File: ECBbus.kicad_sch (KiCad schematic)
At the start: 1 part, among them P1 C96ABC

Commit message: Schematic in progress
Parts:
- removed P1: C96ABC, C96ABCMC, symbol 6x0x-6U-rescue:C96ABC
- added J1, J15, J17, J19, J21: IRQ Selection, Connector_PinHeader_2.54mm:PinHeader_2x06_P2.54mm_Vertical, symbol Connector_Generic:Conn_02x06_Counter_Clockwise
- added J16, J18, J2, J20, J22: Bus_ISA_8bit, Custom:BUSPC_HOST, symbol Custom:Bus_ISA_8bit_CUSTOM
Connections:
- net B_/CLK: now also J16.20 (CLK), J18.20 (CLK), J2.20 (CLK), J20.20 (CLK), J22.20 (CLK)
- net B_/NMI: now also J16.32 (IO), J18.32 (IO), J2.32 (IO), J20.32 (IO), J22.32 (IO)
- net B_A0: now also J16.62 (BA00), J18.62 (BA00), J2.62 (BA00), J20.62 (BA00), J22.62 (BA00)
- net B_A1: now also J16.61 (BA01), J18.61 (BA01), J2.61 (BA01), J20.61 (BA01), J22.61 (BA01)
- net B_A10: now also J16.52 (BA10), J18.52 (BA10), J2.52 (BA10), J20.52 (BA10), J22.52 (BA10)
- net B_A11: now also J16.51 (BA11), J18.51 (BA11), J2.51 (BA11), J20.51 (BA11), J22.51 (BA11)
- net B_A12: now also J16.50 (BA12), J18.50 (BA12), J2.50 (BA12), J20.50 (BA12), J22.50 (BA12)
- net B_A13: now also J16.49 (BA13), J18.49 (BA13), J2.49 (BA13), J20.49 (BA13), J22.49 (BA13)
- net B_A14: now also J16.48 (BA14), J18.48 (BA14), J2.48 (BA14), J20.48 (BA14), J22.48 (BA14)
- net B_A15: now also J16.47 (BA15), J18.47 (BA15), J2.47 (BA15), J20.47 (BA15), J22.47 (BA15)
- net B_A16: now also J16.46 (BA16), J18.46 (BA16), J2.46 (BA16), J20.46 (BA16), J22.46 (BA16)
- net B_A17: now also J16.45 (BA17), J18.45 (BA17), J2.45 (BA17), J20.45 (BA17), J22.45 (BA17)
- net B_A18: now also J16.44 (BA18), J18.44 (BA18), J2.44 (BA18), J20.44 (BA18), J22.44 (BA18)
- net B_A19: now also J16.43 (BA19), J18.43 (BA19), J2.43 (BA19), J20.43 (BA19), J22.43 (BA19)
- net B_A2: now also J16.60 (BA02), J18.60 (BA02), J2.60 (BA02), J20.60 (BA02), J22.60 (BA02)
- net B_A3: now also J16.59 (BA03), J18.59 (BA03), J2.59 (BA03), J20.59 (BA03), J22.59 (BA03)
- net B_A4: now also J16.58 (BA04), J18.58 (BA04), J2.58 (BA04), J20.58 (BA04), J22.58 (BA04)
- net B_A5: now also J16.57 (BA05), J18.57 (BA05), J2.57 (BA05), J20.57 (BA05), J22.57 (BA05)
- net B_A6: now also J16.56 (BA06), J18.56 (BA06), J2.56 (BA06), J20.56 (BA06), J22.56 (BA06)
- net B_A7: now also J16.55 (BA07), J18.55 (BA07), J2.55 (BA07), J20.55 (BA07), J22.55 (BA07)
- net B_A8: now also J16.54 (BA08), J18.54 (BA08), J2.54 (BA08), J20.54 (BA08), J22.54 (BA08)
- net B_A9: now also J16.53 (BA09), J18.53 (BA09), J2.53 (BA09), J20.53 (BA09), J22.53 (BA09)
- net B_D0: now also J16.40 (DB0), J18.40 (DB0), J2.40 (DB0), J20.40 (DB0), J22.40 (DB0)
- net B_D1: now also J16.39 (DB1), J18.39 (DB1), J2.39 (DB1), J20.39 (DB1), J22.39 (DB1)
- net B_D2: now also J16.38 (DB2), J18.38 (DB2), J2.38 (DB2), J20.38 (DB2), J22.38 (DB2)
- net B_D3: now also J16.37 (DB3), J18.37 (DB3), J2.37 (DB3), J20.37 (DB3), J22.37 (DB3)
- net B_D4: now also J16.36 (DB4), J18.36 (DB4), J2.36 (DB4), J20.36 (DB4), J22.36 (DB4)
- net B_D5: now also J16.35 (DB5), J18.35 (DB5), J2.35 (DB5), J20.35 (DB5), J22.35 (DB5)
- net B_D6: now also J16.34 (DB6), J18.34 (DB6), J2.34 (DB6), J20.34 (DB6), J22.34 (DB6)
- net B_D7: now also J16.33 (DB7), J18.33 (DB7), J2.33 (DB7), J20.33 (DB7), J22.33 (DB7)
- net GND: now also J16.1 (GND), J16.10 (GND), J16.31 (GND), J18.1 (GND), J18.10 (GND), J18.31 (GND), J2.1 (GND), J2.10 (GND), J2.31 (GND), J20.1 (GND), J20.10 (GND), J20.31 (GND), J22.1 (GND), J22.10 (GND), J22.31 (GND)
- net VCC: now also J16.29 (VCC), J16.3 (VCC), J18.29 (VCC), J18.3 (VCC), J2.29 (VCC), J2.3 (VCC), J20.29 (VCC), J20.3 (VCC), J22.29 (VCC), J22.3 (VCC)
- new net: J21.10 (Pin_10), J22.23 (IRQ5)
- new net: J21.11 (Pin_11), J22.22 (IRQ6)
- new net: J21.12 (Pin_12), J22.21 (IRQ7)
- new net: J21.8 (Pin_8), J22.25 (IRQ3)
- new net: J21.9 (Pin_9), J22.24 (IRQ4)
- new net: J15.12 (Pin_12), J16.21 (IRQ7)
- new net: J15.11 (Pin_11), J16.22 (IRQ6)
- new net: J15.10 (Pin_10), J16.23 (IRQ5)
- new net: J15.9 (Pin_9), J16.24 (IRQ4)
- new net: J15.8 (Pin_8), J16.25 (IRQ3)
- new net: J1.12 (Pin_12), J2.21 (IRQ7)
- new net: J1.11 (Pin_11), J2.22 (IRQ6)
- new net: J1.10 (Pin_10), J2.23 (IRQ5)
- new net: J1.9 (Pin_9), J2.24 (IRQ4)
- new net: J1.8 (Pin_8), J2.25 (IRQ3)
- new net: J19.10 (Pin_10), J20.23 (IRQ5)
- new net: J19.11 (Pin_11), J20.22 (IRQ6)
- new net: J19.12 (Pin_12), J20.21 (IRQ7)
- new net: J19.8 (Pin_8), J20.25 (IRQ3)
- new net: J19.9 (Pin_9), J20.24 (IRQ4)
- new net: J17.10 (Pin_10), J18.23 (IRQ5)
- new net: J17.11 (Pin_11), J18.22 (IRQ6)
- new net: J17.12 (Pin_12), J18.21 (IRQ7)
- new net: J17.8 (Pin_8), J18.25 (IRQ3)
- new net: J17.9 (Pin_9), J18.24 (IRQ4)
- new net +12V: J16.9 (+12V), J18.9 (+12V), J2.9 (+12V), J20.9 (+12V), J22.9 (+12V)
- new net -12V: J16.7 (-12V), J18.7 (-12V), J2.7 (-12V), J20.7 (-12V), J22.7 (-12V)
- new net -5V: J16.5 (-5V), J18.5 (-5V), J2.5 (-5V), J20.5 (-5V), J22.5 (-5V)
- new net BUSALE: J16.28 (ALE), J18.28 (ALE), J2.28 (ALE), J20.28 (ALE), J22.28 (ALE)
- new net BUSCLK: J16.30 (OSC), J18.30 (OSC), J2.30 (OSC), J20.30 (OSC), J22.30 (OSC)
- new net B_INT: J1.1 (Pin_1), J1.2 (Pin_2), J1.3 (Pin_3), J1.4 (Pin_4), J1.5 (Pin_5), J1.6 (Pin_6), J15.1 (Pin_1), J15.2 (Pin_2), J15.3 (Pin_3), J15.4 (Pin_4), J15.5 (Pin_5), J15.6 (Pin_6), J17.1 (Pin_1), J17.2 (Pin_2), J17.3 (Pin_3), J17.4 (Pin_4), J17.5 (Pin_5), J17.6 (Pin_6), J19.1 (Pin_1), J19.2 (Pin_2), J19.3 (Pin_3), J19.4 (Pin_4), J19.5 (Pin_5), J19.6 (Pin_6), J21.1 (Pin_1), J21.2 (Pin_2), J21.3 (Pin_3), J21.4 (Pin_4), J21.5 (Pin_5), J21.6 (Pin_6)
- new net IOR: J16.14 (~{IOR}), J18.14 (~{IOR}), J2.14 (~{IOR}), J20.14 (~{IOR}), J22.14 (~{IOR})
- new net IOW: J16.13 (~{IOW}), J18.13 (~{IOW}), J2.13 (~{IOW}), J20.13 (~{IOW}), J22.13 (~{IOW})
- new net SMEMR: J16.12 (~{SMEMR}), J18.12 (~{SMEMR}), J2.12 (~{SMEMR}), J20.12 (~{SMEMR}), J22.12 (~{SMEMR})
- new net SMEMW: J16.11 (~{SMEMW}), J18.11 (~{SMEMW}), J2.11 (~{SMEMW}), J20.11 (~{SMEMW}), J22.11 (~{SMEMW})
- new net isa_iq_1: J17.7 (Pin_7), J18.4 (IRQ2)
- new net isa_iq_2: J15.7 (Pin_7), J16.4 (IRQ2)
- new net isa_iq_3: J1.7 (Pin_7), J2.4 (IRQ2)
- new net isa_iq_4: J19.7 (Pin_7), J20.4 (IRQ2)
- new net isa_iq_5: J21.7 (Pin_7), J22.4 (IRQ2)
- new net /RESET: J16.2 (RESET), J18.2 (RESET), J2.2 (RESET), J20.2 (RESET), J22.2 (RESET)
- no-connect marks 41 -> 55
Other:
- company: N8VEM Users Group -> (none)
- title: 6809 and 6502 ATX and 6U -> 6809PC

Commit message: PCB in progress
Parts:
- J1: renamed from J21; footprint Connector_PinHeader_2.54mm:PinHeader_2x06_P2.54mm_Vertical -> Custom:STD_DDW_PINHEAD_V_2x06
- J2: renamed from J17; footprint Connector_PinHeader_2.54mm:PinHeader_2x06_P2.54mm_Vertical -> Custom:STD_DDW_PINHEAD_V_2x06
- J5: renamed from J15; footprint Connector_PinHeader_2.54mm:PinHeader_2x06_P2.54mm_Vertical -> Custom:STD_DDW_PINHEAD_V_2x06
- J7: renamed from J1; footprint Connector_PinHeader_2.54mm:PinHeader_2x06_P2.54mm_Vertical -> Custom:STD_DDW_PINHEAD_V_2x06
- J9: renamed from J19; footprint Connector_PinHeader_2.54mm:PinHeader_2x06_P2.54mm_Vertical -> Custom:STD_DDW_PINHEAD_V_2x06
- renumbered J20 to J10, J22 to J3, J18 to J4, J16 to J6, J2 to J8

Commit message: PCB
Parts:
- J1, J2, J5, J7, J9: symbol Connector_Generic:Conn_02x06_Counter_Clockwise -> Connector_Generic:Conn_02x06_Odd_Even
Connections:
- net B_INT: now also J1.11 (Pin_11), J1.7 (Pin_7), J1.9 (Pin_9), J2.11 (Pin_11), J2.7 (Pin_7), J2.9 (Pin_9), J5.11 (Pin_11), J5.7 (Pin_7), J5.9 (Pin_9), J7.11 (Pin_11), J7.7 (Pin_7), J7.9 (Pin_9), J9.11 (Pin_11), J9.7 (Pin_7), J9.9 (Pin_9); no longer J1.2 (Pin_2), J1.4 (Pin_4), J1.6 (Pin_6), J2.2 (Pin_2), J2.4 (Pin_4), J2.6 (Pin_6), J5.2 (Pin_2), J5.4 (Pin_4), J5.6 (Pin_6), J7.2 (Pin_2), J7.4 (Pin_4), J7.6 (Pin_6), J9.2 (Pin_2), J9.4 (Pin_4), J9.6 (Pin_6)
- net isa_iq_1: now also J2.12 (Pin_12); no longer J2.7 (Pin_7)
- net isa_iq_2: now also J5.12 (Pin_12); no longer J5.7 (Pin_7)
- net isa_iq_3: now also J7.12 (Pin_12); no longer J7.7 (Pin_7)
- net isa_iq_4: now also J9.12 (Pin_12); no longer J9.7 (Pin_7)
- net isa_iq_5: now also J1.12 (Pin_12); no longer J1.7 (Pin_7)
- net at J1.10 (Pin_10): now also J3.25 (IRQ3); no longer J3.23 (IRQ5)
- net at J3.22 (IRQ6): now also J1.4 (Pin_4); no longer J1.11 (Pin_11)
- net at J3.21 (IRQ7): now also J1.2 (Pin_2); no longer J1.12 (Pin_12)
- net at J1.8 (Pin_8): now also J3.24 (IRQ4); no longer J3.25 (IRQ3)
- net at J6.21 (IRQ7): now also J5.2 (Pin_2); no longer J5.12 (Pin_12)
- net at J6.22 (IRQ6): now also J5.4 (Pin_4); no longer J5.11 (Pin_11)
- net at J6.23 (IRQ5): now also J5.6 (Pin_6); no longer J5.10 (Pin_10)
- net at J6.24 (IRQ4): now also J5.8 (Pin_8); no longer J5.9 (Pin_9)
- net at J6.25 (IRQ3): now also J5.10 (Pin_10); no longer J5.8 (Pin_8)
- net at J8.21 (IRQ7): now also J7.2 (Pin_2); no longer J7.12 (Pin_12)
- net at J8.22 (IRQ6): now also J7.4 (Pin_4); no longer J7.11 (Pin_11)
- net at J8.23 (IRQ5): now also J7.6 (Pin_6); no longer J7.10 (Pin_10)
- net at J8.24 (IRQ4): now also J7.8 (Pin_8); no longer J7.9 (Pin_9)
- net at J8.25 (IRQ3): now also J7.10 (Pin_10); no longer J7.8 (Pin_8)
- net at J9.10 (Pin_10): now also J10.25 (IRQ3); no longer J10.23 (IRQ5)
- net at J10.22 (IRQ6): now also J9.4 (Pin_4); no longer J9.11 (Pin_11)
- net at J10.21 (IRQ7): now also J9.2 (Pin_2); no longer J9.12 (Pin_12)
- net at J9.8 (Pin_8): now also J10.24 (IRQ4); no longer J10.25 (IRQ3)
- net at J2.10 (Pin_10): now also J4.25 (IRQ3); no longer J4.23 (IRQ5)
- net at J4.22 (IRQ6): now also J2.4 (Pin_4); no longer J2.11 (Pin_11)
- net at J4.21 (IRQ7): now also J2.2 (Pin_2); no longer J2.12 (Pin_12)
- net at J2.8 (Pin_8): now also J4.24 (IRQ4); no longer J4.25 (IRQ3)
- new net: J1.6 (Pin_6), J3.23 (IRQ5)
- new net: J10.23 (IRQ5), J9.6 (Pin_6)
- new net: J2.6 (Pin_6), J4.23 (IRQ5)
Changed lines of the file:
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@@
 	)
 	(symbol
-		(lib_id "Connector_Generic:Conn_02x06_Counter_Clockwise")
+		(lib_id "Connector_Generic:Conn_02x06_Odd_Even")
 		(at 35.56 177.8 0)
 		(unit 1)
@@
 			)
 		)
-		(property "Description" "Generic connector, double row, 02x06, counter clockwise pin numbering scheme (similar to DIP package numbering), script generated (kicad-library-utils/schlib/autogen/connector/)"
+		(property "Description" "Generic connector, double row, 02x06, odd/even pin numbering scheme (row 1 odd numbers, row 2 even numbers), script generated (kicad-library-utils/schlib/autogen/connector/)"
 			(at 35.56 177.8 0)
 			(effects
@@
 	)
 	(symbol
-		(lib_id "Connector_Generic:Conn_02x06_Counter_Clockwise")
+		(lib_id "Connector_Generic:Conn_02x06_Odd_Even")
 		(at 322.58 78.74 0)
 		(unit 1)
@@
 			)
 		)
-		(property "Description" "Generic connector, double row, 02x06, counter clockwise pin numbering scheme (similar to DIP package numbering), script generated (kicad-library-utils/schlib/autogen/connector/)"
+		(property "Description" "Generic connector, double row, 02x06, odd/even pin numbering scheme (row 1 odd numbers, row 2 even numbers), script generated (kicad-library-utils/schlib/autogen/connector/)"
 			(at 322.58 78.74 0)
 			(effects
@@
 	)
 	(symbol
-		(lib_id "Connector_Generic:Conn_02x06_Counter_Clockwise")
+		(lib_id "Connector_Generic:Conn_02x06_Odd_Even")
 		(at 226.06 78.74 0)
 		(unit 1)
@@
 			)
 		)
-		(property "Description" "Generic connector, double row, 02x06, counter clockwise pin numbering scheme (similar to DIP package numbering), script generated (kicad-library-utils/schlib/autogen/connector/)"
+		(property "Description" "Generic connector, double row, 02x06, odd/even pin numbering scheme (row 1 odd numbers, row 2 even numbers), script generated (kicad-library-utils/schlib/autogen/connector/)"
 			(at 226.06 78.74 0)
 			(effects
@@
 	)
 	(symbol
-		(lib_id "Connector_Generic:Conn_02x06_Counter_Clockwise")
+		(lib_id "Connector_Generic:Conn_02x06_Odd_Even")
 		(at 36.83 81.28 0)
 		(unit 1)
@@
 			)
 		)
-		(property "Description" "Generic connector, double row, 02x06, counter clockwise pin numbering scheme (similar to DIP package numbering), script generated (kicad-library-utils/schlib/autogen/connector/)"
+		(property "Description" "Generic connector, double row, 02x06, odd/even pin numbering scheme (row 1 odd numbers, row 2 even numbers), script generated (kicad-library-utils/schlib/autogen/connector/)"
 			(at 36.83 81.28 0)
 			(effects
@@
 	)
 	(symbol
-		(lib_id "Connector_Generic:Conn_02x06_Counter_Clockwise")
+		(lib_id "Connector_Generic:Conn_02x06_Odd_Even")
 		(at 130.81 80.01 0)
 		(unit 1)
@@
 			)
 		)
-		(property "Description" "Generic connector, double row, 02x06, counter clockwise pin numbering scheme (similar to DIP package numbering), script generated (kicad-library-utils/schlib/autogen/connector/)"
+		(property "Description" "Generic connector, double row, 02x06, odd/even pin numbering scheme (row 1 odd numbers, row 2 even numbers), script generated (kicad-library-utils/schlib/autogen/connector/)"
 			(at 130.81 80.01 0)
 			(effects

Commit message: V1.1
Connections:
- net TC: now reaches J3.27 (TC)
- net TC: now also J10.27 (TC), J4.27 (TC), J6.27 (TC), J8.27 (TC)
- no-connect marks 55 -> 50
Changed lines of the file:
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@@
 	)
 	(no_connect
-		(at 64.77 91.44)
-	)
-	(no_connect
 		(at 63.5 165.1)
 	)
@@
 	)
 	(no_connect
-		(at 350.52 88.9)
-	)
-	(no_connect
 		(at 64.77 43.18)
 	)
@@
 	)
 	(no_connect
-		(at 158.75 90.17)
-	)
-	(no_connect
 		(at 350.52 58.42)
 	)
@@
 	)
 	(no_connect
-		(at 63.5 187.96)
-	)
-	(no_connect
-		(at 254 88.9)
-	)
-	(no_connect
 		(at 100.33 48.26)
 	)
@@
 	(wire
 		(pts
+			(xy 62.23 91.44) (xy 64.77 91.44)
+		)
+		(stroke
+			(width 0)
+			(type default)
+		)
+	)
+	(wire
+		(pts
 			(xy 99.06 167.64) (xy 102.87 167.64)
 		)
@@
 	(wire
 		(pts
+			(xy 251.46 88.9) (xy 254 88.9)
+		)
+		(stroke
+			(width 0)
+			(type default)
+		)
+	)
+	(wire
+		(pts
 			(xy 289.56 99.06) (xy 293.37 99.06)
 		)
@@
 	(wire
 		(pts
+			(xy 156.21 90.17) (xy 158.75 90.17)
+		)
+		(stroke
+			(width 0)
+			(type default)
+		)
+	)
+	(wire
+		(pts
 			(xy 43.18 182.88) (xy 63.5 182.88)
 		)
@@
 	(wire
 		(pts
+			(xy 60.96 187.96) (xy 63.5 187.96)
+		)
+		(stroke
+			(width 0)
+			(type default)
+		)
+	)
+	(wire
+		(pts
 			(xy 330.2 99.06) (xy 350.52 99.06)
 		)
@@
 	(wire
 		(pts
+			(xy 347.98 88.9) (xy 350.52 88.9)
+		)
+		(stroke
+			(width 0)
+			(type default)
+		)
+	)
+	(wire
+		(pts
 			(xy 60.96 170.18) (xy 63.5 170.18)
 		)
@@
 		)
 	)
+	(global_label "TC"
+		(shape input)
+		(at 156.21 90.17 180)
+		(fields_autoplaced yes)
+		(effects
+			(font
+				(size 1.27 1.27)
+			)
+			(justify right)
+		)
+		(property "Intersheetrefs" "${INTERSHEET_REFS}"
+			(at 151.6414 90.17 0)
+			(effects
+				(font
+					(size 1.27 1.27)
+				)
+				(justify right)
+				(hide yes)
+			)
+		)
+	)
 	(global_label "B_D3"
 		(shape bidirectional)
@@
 		)
 	)
+	(global_label "TC"
+		(shape input)
+		(at 251.46 88.9 180)
+		(fields_autoplaced yes)
+		(effects
+			(font
+				(size 1.27 1.27)
+			)
+			(justify right)
+		)
+		(property "Intersheetrefs" "${INTERSHEET_REFS}"
+			(at 246.8914 88.9 0)
+			(effects
+				(font
+					(size 1.27 1.27)
+				)
+				(justify right)
+				(hide yes)
+			)
+		)
+	)
 	(global_label "B_A6"
 		(shape bidirectional)
@@
 		)
 	)
+	(global_label "TC"
+		(shape input)
+		(at 60.96 187.96 180)
+		(fields_autoplaced yes)
+		(effects
+			(font
+				(size 1.27 1.27)
+			)
+			(justify right)
+		)
+		(property "Intersheetrefs" "${INTERSHEET_REFS}"
+			(at 56.3914 187.96 0)
+			(effects
+				(font
+					(size 1.27 1.27)
+				)
+				(justify right)
+				(hide yes)
+			)
+		)
+	)
 	(global_label "B_A15"
 		(shape tri_state)
@@
 		)
 	)
+	(global_label "TC"
+		(shape input)
+		(at 347.98 88.9 180)
+		(fields_autoplaced yes)
+		(effects
+			(font
+				(size 1.27 1.27)
+			)
+			(justify right)
+		)
+		(property "Intersheetrefs" "${INTERSHEET_REFS}"
+			(at 343.4114 88.9 0)
+			(effects
+				(font
+					(size 1.27 1.27)
+				)
+				(justify right)
+				(hide yes)
+			)
+		)
+	)
 	(global_label "B_A0"
 		(shape bidirectional)
@@
 				(hide yes)
 			)
+		)
+	)
+	(global_label "TC"
+		(shape input)
+		(at 62.23 91.44 180)
+		(fields_autoplaced yes)
+		(effects
+			(font
+				(size 1.27 1.27)
+			)
+			(justify right)
+		)
+		(property "Intersheetrefs" "${INTERSHEET_REFS}"
+			(at 57.6614 91.44 0)
+			(effects
+				(font
+					(size 1.27 1.27)
+				)
+				(justify right)
+				(hide yes)
+			)

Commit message: 6809PC work
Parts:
- added J13: IRQ Selection, Custom:STD_DDW_PINHEAD_V_2x06, symbol Connector_Generic:Conn_02x06_Odd_Even
- added J14: Bus_ISA_8bit, Custom:BUSPC_HOST, symbol Custom:Bus_ISA_8bit_CUSTOM
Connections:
- net +12V: now also J14.9 (+12V)
- net -12V: now also J14.7 (-12V)
- net -5V: now also J14.5 (-5V)
- net BUSALE: now also J14.28 (ALE)
- net BUSCLK: now also J14.30 (OSC)
- net B_/CLK: now also J14.20 (CLK)
- net B_/NMI: now also J14.32 (IO)
- net B_A0: now also J14.62 (BA00)
- net B_A1: now also J14.61 (BA01)
- net B_A10: now also J14.52 (BA10)
- net B_A11: now also J14.51 (BA11)
- net B_A12: now also J14.50 (BA12)
- net B_A13: now also J14.49 (BA13)
- net B_A14: now also J14.48 (BA14)
- net B_A15: now also J14.47 (BA15)
- net B_A16: now also J14.46 (BA16)
- net B_A17: now also J14.45 (BA17)
- net B_A18: now also J14.44 (BA18)
- net B_A19: now also J14.43 (BA19)
- net B_A2: now also J14.60 (BA02)
- net B_A3: now also J14.59 (BA03)
- net B_A4: now also J14.58 (BA04)
- net B_A5: now also J14.57 (BA05)
- net B_A6: now also J14.56 (BA06)
- net B_A7: now also J14.55 (BA07)
- net B_A8: now also J14.54 (BA08)
- net B_A9: now also J14.53 (BA09)
- net B_D0: now also J14.40 (DB0)
- net B_D1: now also J14.39 (DB1)
- net B_D2: now also J14.38 (DB2)
- net B_D3: now also J14.37 (DB3)
- net B_D4: now also J14.36 (DB4)
- net B_D5: now also J14.35 (DB5)
- net B_D6: now also J14.34 (DB6)
- net B_D7: now also J14.33 (DB7)
- net B_INT: now also J13.1 (Pin_1), J13.11 (Pin_11), J13.3 (Pin_3), J13.5 (Pin_5), J13.7 (Pin_7), J13.9 (Pin_9)
- net GND: now also J10.42 (AEN), J3.42 (AEN), J4.42 (AEN), J6.42 (AEN), J8.42 (AEN), J14.1 (GND), J14.10 (GND), J14.31 (GND), J14.42 (AEN)
- net IOR: now also J14.14 (~{IOR})
- net IOW: now also J14.13 (~{IOW})
- net SMEMR: now also J14.12 (~{SMEMR})
- net SMEMW: now also J14.11 (~{SMEMW})
- net TC: now also J14.27 (TC)
- net VCC: now also J14.29 (VCC), J14.3 (VCC)
- net isa_iq_5: now also J13.12 (Pin_12), J14.4 (IRQ2)
- net /RESET: now also J14.2 (RESET)
- new net: J13.10 (Pin_10), J14.25 (IRQ3)
- new net: J13.2 (Pin_2), J14.21 (IRQ7)
- new net: J13.4 (Pin_4), J14.22 (IRQ6)
- new net: J13.6 (Pin_6), J14.23 (IRQ5)
- new net: J13.8 (Pin_8), J14.24 (IRQ4)
- no-connect marks 50 -> 54

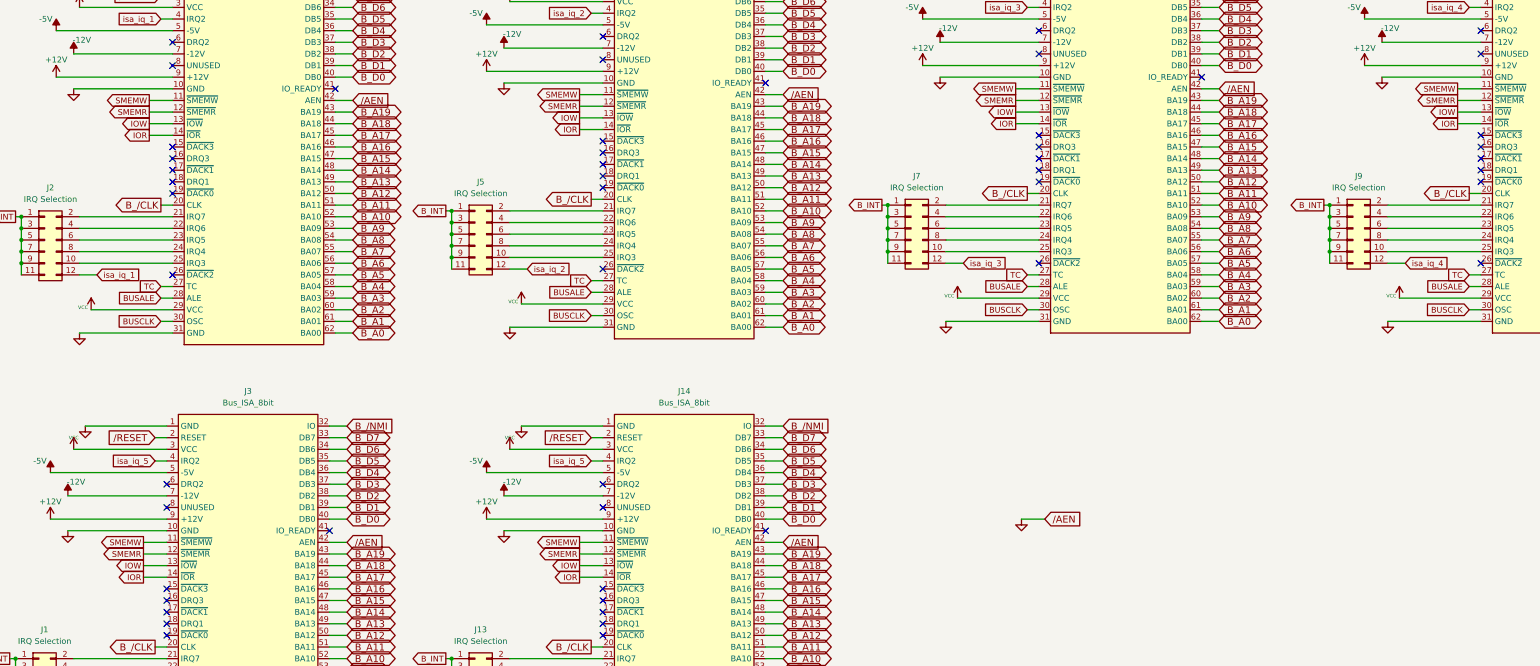
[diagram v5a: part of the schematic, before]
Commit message: fix issue with ISA RW select lines
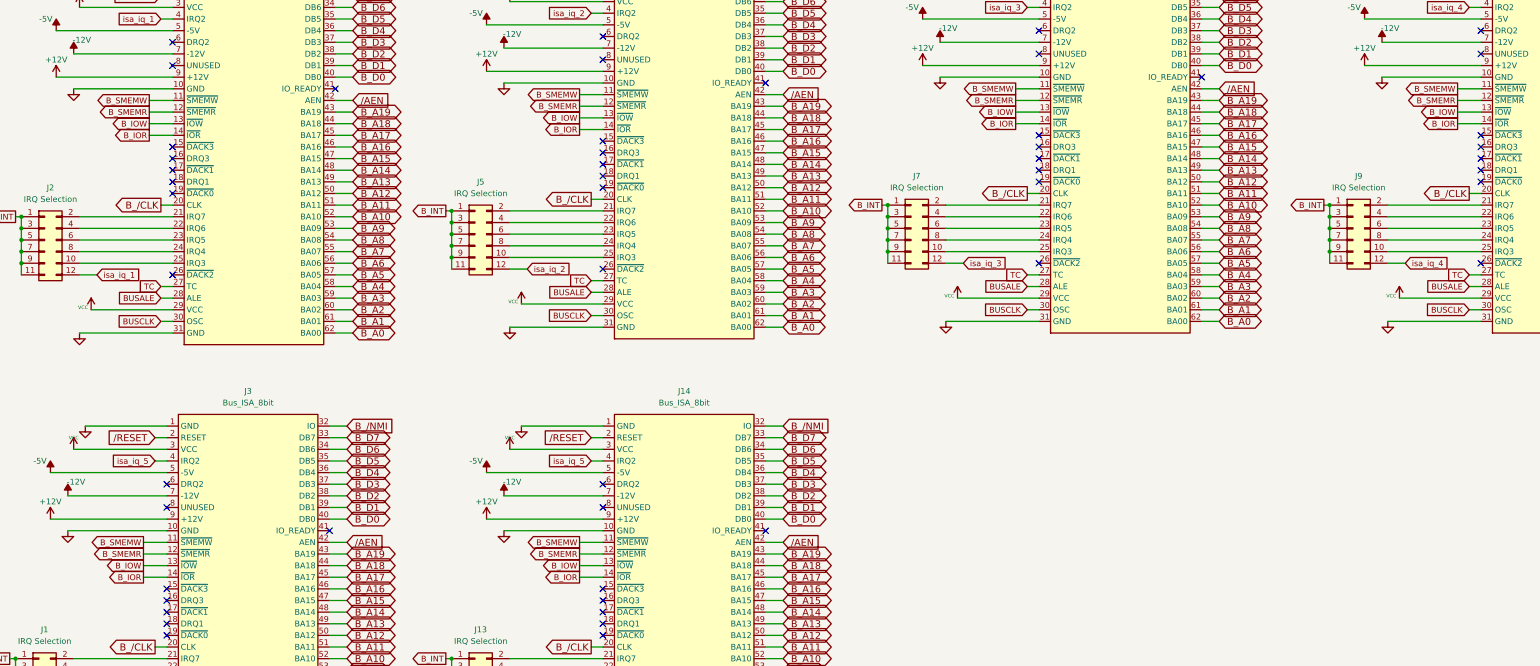
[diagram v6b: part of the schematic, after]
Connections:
- net GND: no longer J10.42 (AEN), J14.42 (AEN), J3.42 (AEN), J4.42 (AEN), J6.42 (AEN), J8.42 (AEN)
- net IOR renamed B_IOR
- net IOW renamed B_IOW
- net SMEMR renamed B_SMEMR
- net SMEMW renamed B_SMEMW
- new net /AEN: J10.42 (AEN), J14.42 (AEN), J3.42 (AEN), J4.42 (AEN), J6.42 (AEN), J8.42 (AEN)
